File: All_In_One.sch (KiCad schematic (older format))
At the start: 102 parts, among them J1 MS_jumper_xaxis, J10 Motors, J11 Fan, J2 MS_jumper_yaxis, J3 Base_Proxy, J4 Water_Pump, J5 MS_jumper, J6 Stepper_xaxis, J7 servo_motor, J8 ARM PROXY, J9 bluetooth, Q1 BC547, U1 Prashant_library_Arduino_Mega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, U10 PC817, U11 PC817, U12 PC817, U13 PC817, U14 5V_Regulator, U15 PC817, U16 PC817, U17 PC817, U2 L298, U3 L298, U4 5V_Regulator, U5 PC817, U6 PC817, U7 PC817, U8 PC817, U9 PC817

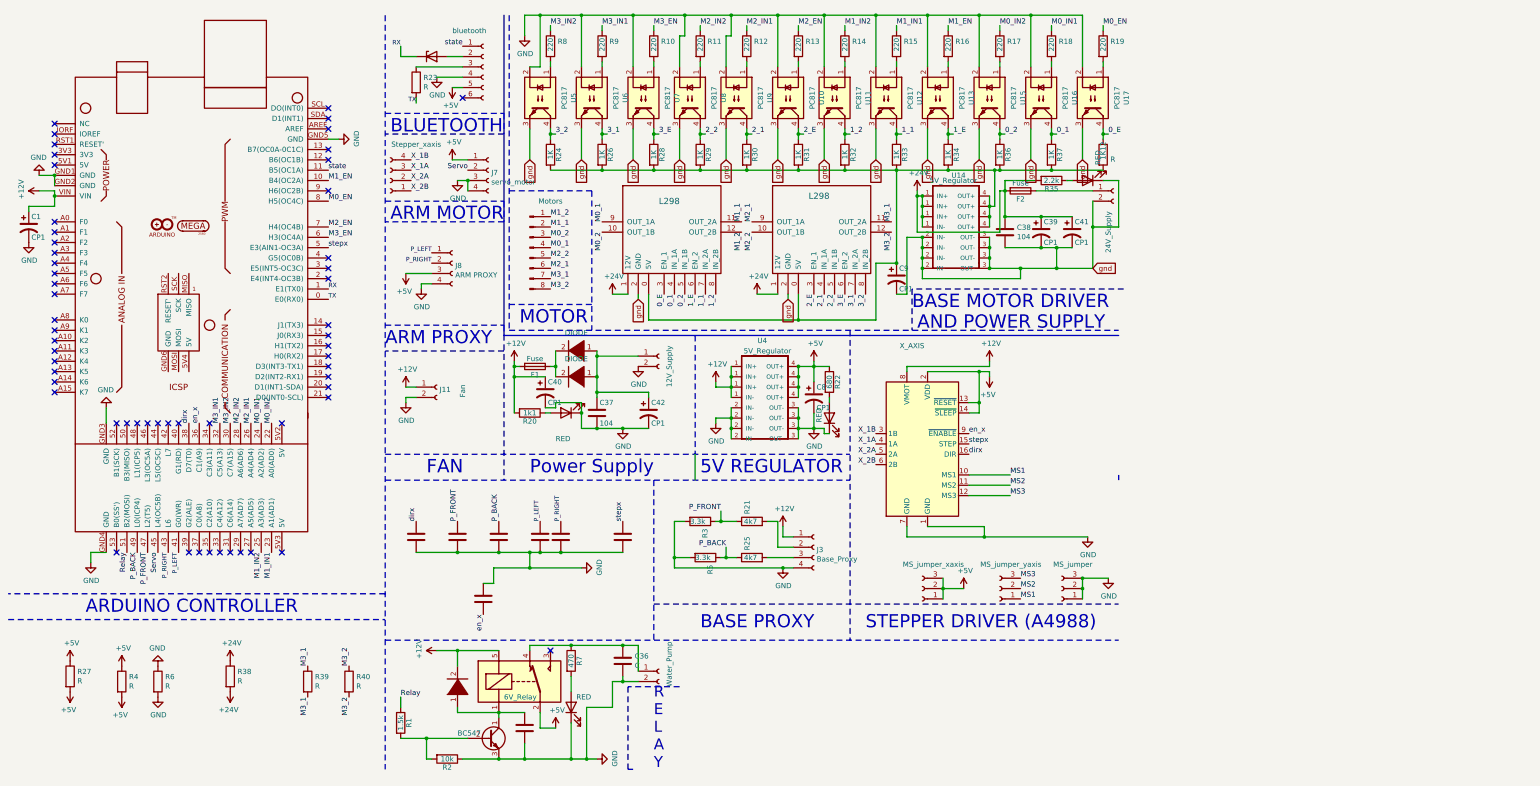
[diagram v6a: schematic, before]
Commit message: battery indicator
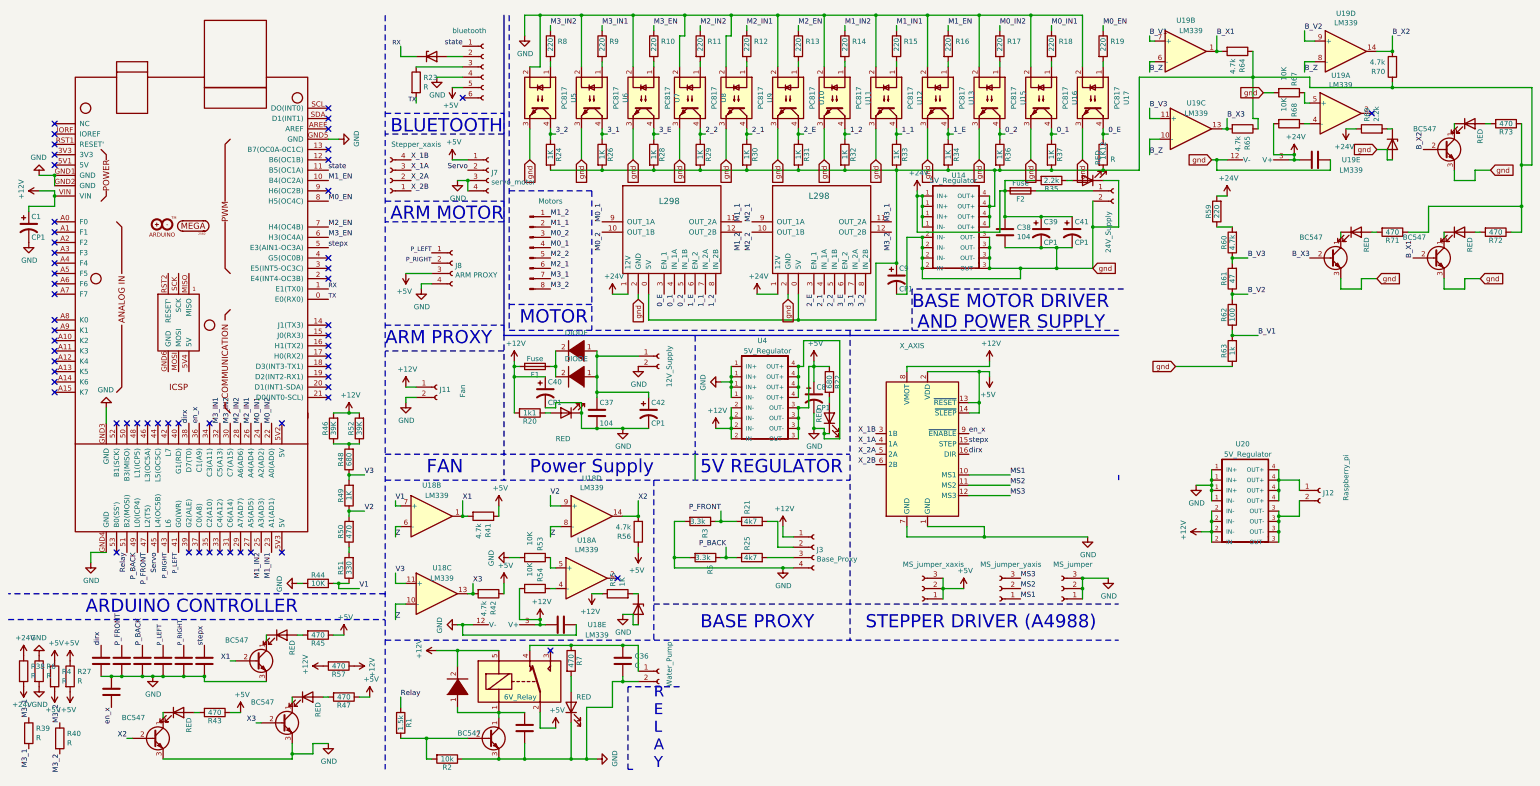
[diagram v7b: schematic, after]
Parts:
- added C4, C6: C, modFiles:Capacitor_Disc_Small, symbol Device:C
- added D12, D14: D_Zener, Diode_THT:D_T-1_P5.08mm_Horizontal, symbol Device:D_Zener
- added D13, D15, D16, D4, D5, D6: RED, modFiles:LED_D3.0mm, symbol Device:LED
- added J12: Raspberry_pi, 0_18:New_conn_1x2, symbol Connector:Conn_01x02_Female
- added Q2, Q3, Q4, Q5, Q6, Q7: BC547, Package_TO_SOT_THT:TO-92_Inline, symbol Transistor_BJT:BC547
- added R41, R42, R56, R60, R64, R65, R70: 4.7k, modFiles:Resistor_small, symbol Device:R
- added R43, R45, R47, R50, R57, R71, R72, R73: 470, modFiles:Resistor_small, symbol Device:R
- added R44, R53, R54, R67, R68: 10K, modFiles:Resistor_small, symbol Device:R
- added R46, R52: 39K, modFiles:Resistor_small, symbol Device:R
- added R48: 680, modFiles:Resistor_small, symbol Device:R
- added R49, R55: 1K, modFiles:Resistor_small, symbol Device:R
- added R51: 330, modFiles:Resistor_small, symbol Device:R
- added R59: 220, modFiles:Resistor_small, symbol Device:R
- added R61: 47, modFiles:Resistor_small, symbol Device:R
- added R62: 100, modFiles:Resistor_small, symbol Device:R
- added R63: 1k, modFiles:Resistor_small, symbol Device:R
- added R69: 2.2k, modFiles:Resistor_small, symbol Device:R
- added U18, U19: LM339, Package_DIP:DIP-14_W7.62mm_LongPads, symbol Comparator:LM339
- added U20: 5V_Regulator, modFiles:Buck_5A, symbol BUCK_Controller:BUCK
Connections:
- net +12V: now also U4.2 (IN-), C4.2, R46.2, R52.2, R54.2, R55.1, R57.1, R57.2, U18.3 (V+), U20.2 (IN-); no longer U4.1 (IN-)
- net +24V: now also C6.2, R59.2, R68.2, R69.1, U19.3 (V+)
- net +5V: now also U4.3 (OUT-), R41.1, R42.1, R43.1, R45.1, R47.1, R56.1; no longer U4.4 (OUT+)
- net GND: now also U4.1 (IN-), U4.4 (OUT+), C4.1, D12.2 (A), Q2.3 (E), Q3.3 (E), Q4.3 (E), R44.1, R53.2, U18.12 (V-), U20.1 (IN-); no longer U4.2 (IN-), U4.3 (OUT-)
- net gnd: now also C6.1, D14.2 (A), Q5.3 (E), Q6.3 (E), Q7.3 (E), R63.1, R67.2, U19.12 (V-)
- net at 1K12.2, C9.1, R24.2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: now also R64.1, R65.1, R70.1, R71.1, R72.1, R73.1
- new net: R54.1, U18.4 (-)
- new net: R53.1, U18.5 (+)
- new net: J12.2 (Pin_2), U20.3 (OUT-)
- new net: J12.1 (Pin_1), U20.4 (OUT+)
- new net: R68.1, U19.4 (-)
- new net: R67.1, U19.5 (+)
- new net: D14.1 (K), R69.2
- new net: R59.1, R60.2
- new net: D15.1 (K), Q6.1 (C)
- new net: D15.2 (A), R72.2
- new net: D13.1 (K), Q5.1 (C)
- new net: D13.2 (A), R71.2
- new net: D16.1 (K), Q7.1 (C)
- new net: D16.2 (A), R73.2
- new net: D12.1 (K), R55.2
- new net: D5.1 (K), Q3.1 (C)
- new net: D5.2 (A), R45.2
- new net: D6.1 (K), Q4.1 (C)
- new net: D6.2 (A), R47.2
- new net: D4.1 (K), Q2.1 (C)
- new net: D4.2 (A), R43.2
- new net: R46.1, R48.2, R52.1
- new net: R50.1, R51.2
- new net B_V1: R62.1, R63.2, U19.7 (+)
- new net B_V2: R61.1, R62.2, U19.9 (+)
- new net B_V3: R60.1, R61.2, U19.11 (+)
- new net B_X1: Q6.2 (B), R64.2, U19.1
- new net B_X2: Q7.2 (B), R70.2, U19.14
- new net B_X3: Q5.2 (B), R65.2, U19.13
- new net B_Z: U19.10 (-), U19.6 (-), U19.8 (-)
- new net V1: R44.2, R51.1, U18.7 (+)
- new net V2: R49.1, R50.2, U18.9 (+)
- new net V3: R48.1, R49.2, U18.11 (+)
- new net X1: Q3.2 (B), R41.2, U18.1
- new net X2: Q2.2 (B), R56.2, U18.14
- new net X3: Q4.2 (B), R42.2, U18.13
- new net Z: U18.10 (-), U18.6 (-), U18.8 (-)
- no-connect marks 58 -> 60
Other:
- moved on the sheet: R38, R39, R4, R40, R6

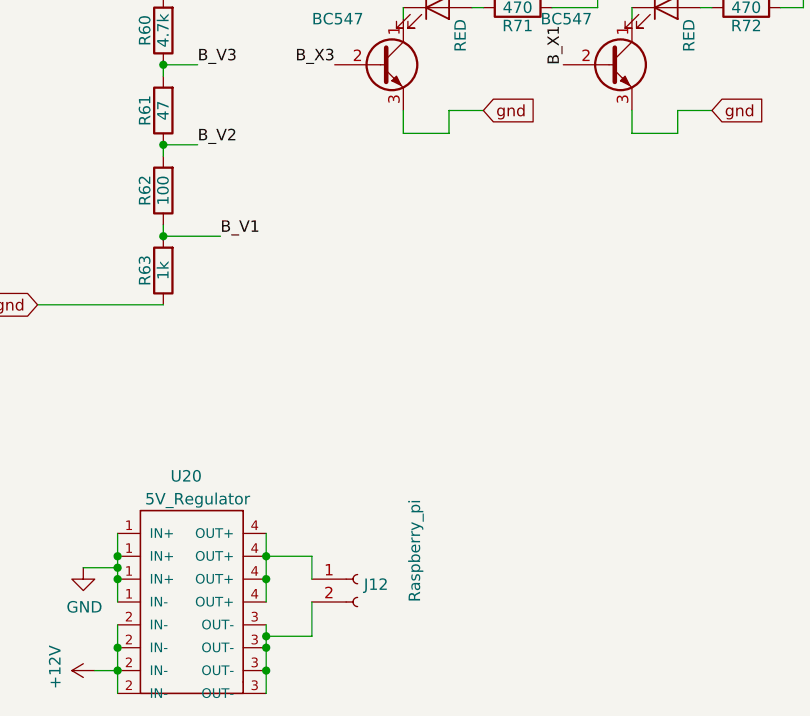
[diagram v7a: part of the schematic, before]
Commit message: added buck for pi
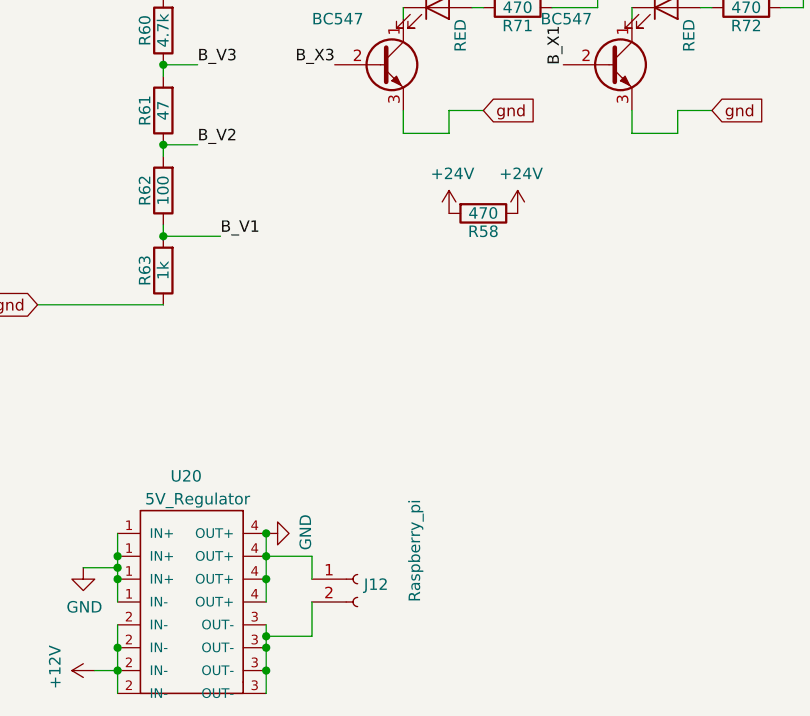
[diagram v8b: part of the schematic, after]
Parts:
- added R58: 470, modFiles:Resistor_small, symbol Device:R
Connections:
- net +24V: now also R58.1, R58.2
- net GND: now also J12.1 (Pin_1), U20.4 (OUT+)
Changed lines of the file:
@@
 	8100 4300 8200 4300
 Connection ~ 8100 4300
+$Comp
+L power:GND #PWR048
+U 1 1 5F3FEFCC
+P 12750 4900
+F 0 "#PWR048" H 12750 4650 50  0001 C CNN
+F 1 "GND" H 12755 4727 50  0000 C CNN
+F 2 "" H 12750 4900 50  0001 C CNN
+F 3 "" H 12750 4900 50  0001 C CNN
+	1    12750 4900
+	0    -1   -1   0
+$EndComp
+Connection ~ 12750 4900
+$Comp
+L Device:R R58
+U 1 1 5F400AD9
+P 13700 3500
+F 0 "R58" V 13780 3500 50  0000 C CNN
+F 1 "470" V 13700 3500 50  0000 C CNN
+F 2 "modFiles:Resistor_small" V 13630 3500 50  0001 C CNN
+F 3 "~" H 13700 3500 50  0001 C CNN
+	1    13700 3500
+	0    1    1    0
+$EndComp
+$Comp
+L power:+24V #PWR049
+U 1 1 5F401689
+P 13550 3500
+F 0 "#PWR049" H 13550 3350 50  0001 C CNN
+F 1 "+24V" H 13565 3673 50  0000 C CNN
+F 2 "" H 13550 3500 50  0001 C CNN
+F 3 "" H 13550 3500 50  0001 C CNN
+	1    13550 3500
+	1    0    0    -1
+$EndComp
+$Comp
+L power:+24V #PWR050
+U 1 1 5F401A9F
+P 13850 3500
+F 0 "#PWR050" H 13850 3350 50  0001 C CNN
+F 1 "+24V" H 13865 3673 50  0000 C CNN
+F 2 "" H 13850 3500 50  0001 C CNN
+F 3 "" H 13850 3500 50  0001 C CNN
+	1    13850 3500
+	1    0    0    -1
+$EndComp
 $EndSCHEMATC
